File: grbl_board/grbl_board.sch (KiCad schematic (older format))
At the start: 0 parts

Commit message: finished GRBL controller
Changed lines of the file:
@@
 $Descr A4 11693 8268
 encoding utf-8
-Sheet 1 3
+Sheet 1 4
 Title ""
 Date ""
@@
 $EndDescr
 $Sheet
-S 2550 2700 1700 1700
+S 3500 3800 1700 1700
 U 61764DEB
 F0 "grbl_controller" 50
 F1 "grbl_controller.sch" 50
+F2 "RESET" I L 3500 5300 50
+F3 "DIR_X" I R 5200 4000 50
+F4 "DIR_Y" I R 5200 4100 50
+F5 "DIR_Z" I R 5200 4200 50
+F6 "STEP_X" I R 5200 4450 50
+F7 "STEP_Y" I R 5200 4550 50
+F8 "STEP_Z" I R 5200 4650 50
+F9 "LIM_X" I R 5200 4900 50
+F10 "LIM_Y" I R 5200 5000 50
+F11 "LIM_Z" I R 5200 5100 50
+F12 "SPINDLE_DIR" I L 3500 4450 50
+F13 "STEPPER_EN" I R 5200 5300 50
+F14 "COOL_MIST" I L 3500 4100 50
+F15 "RSTABRT" I L 3500 4900 50
+F16 "HOLD" I L 3500 5000 50
+F17 "START" I L 3500 5100 50
+F18 "DOOR_SAFETY" I L 3500 4800 50
+F19 "PROBE" I L 3500 3900 50
+F20 "COOL_FLOOD" I L 3500 4200 50
+F21 "SPINDLE_EN" I L 3500 4550 50
+F22 "SPINDLE_PWM" I L 3500 4350 50
 $EndSheet
 $Sheet
-S 7050 2650 1800 1700
+S 7300 2550 1700 1700
 U 61764E0B
 F0 "stepper_drivers" 50
 F1 "stepper_drivers.sch" 50
 $EndSheet
+$Sheet
+S 3500 1350 1700 1700
+U 619755E7
+F0 "power_supply" 50
+F1 "power_supply.sch" 50
+$EndSheet
 $EndSCHEMATC

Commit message: power supply stage
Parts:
- added J?: 12VDC, symbol Connector:Screw_Terminal_01x02
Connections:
- new net 12VDC: J?.2 (Pin_2)
- new net GND: J?.1 (Pin_1)
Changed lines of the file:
@@
 F0 "power_supply" 50
 F1 "power_supply.sch" 50
+F2 "32VDC" I R 5200 1650 50
+F3 "12VDC" I R 5200 1850 50
+F4 "5VDC" I R 5200 2050 50
 $EndSheet
+$Comp
+L Connector:Screw_Terminal_01x02 J?
+U 1 1 6181440B
+P 1750 1700
+F 0 "J?" H 1668 1375 50  0000 C CNN
+F 1 "12VDC" H 1668 1466 50  0000 C CNN
+F 2 "" H 1750 1700 50  0001 C CNN
+F 3 "~" H 1750 1700 50  0001 C CNN
+	1    1750 1700
+	-1   0    0    1
+$EndComp
+Text Label 5200 1850 0    50   ~ 0
+12VDC
+Text Label 1950 1600 0    50   ~ 0
+12VDC
+$Comp
+L power:GND #PWR?
+U 1 1 61816450
+P 2050 1750
+F 0 "#PWR?" H 2050 1500 50  0001 C CNN
+F 1 "GND" H 2055 1577 50  0000 C CNN
+F 2 "" H 2050 1750 50  0001 C CNN
+F 3 "" H 2050 1750 50  0001 C CNN
+	1    2050 1750
+	1    0    0    -1
+$EndComp
+Wire Wire Line
+	2050 1750 2050 1700
+Wire Wire Line
+	2050 1700 1950 1700
 $EndSCHEMATC

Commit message: motor driver and mcu and limit switches
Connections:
- net 12VDC renamed +12V
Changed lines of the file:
@@
 $Descr A4 11693 8268
 encoding utf-8
-Sheet 1 4
+Sheet 1 6
 Title ""
 Date ""
@@
 $EndSheet
 $Sheet
-S 7300 2550 1700 1700
+S 7050 2450 1700 1700
 U 61764E0B
-F0 "stepper_drivers" 50
-F1 "stepper_drivers.sch" 50
+F0 "aux_mcu" 50
+F1 "aux_mcu.sch" 50
+F2 "X_STEP" I L 7050 2550 50
+F3 "Y_STEP" I L 7050 2650 50
+F4 "Z_STEP" I L 7050 2750 50
+F5 "X_DIR" I L 7050 2900 50
+F6 "Y_DIR" I L 7050 3000 50
+F7 "Z_DIR" I L 7050 3100 50
+F8 "LIM0_IN" I R 8750 3500 50
+F9 "LIM1_IN" I R 8750 3600 50
+F10 "LIM_OUT" I R 8750 3700 50
+F11 "E_DIR_OUT" I R 8750 3300 50
+F12 "X_STEP_OUT" I R 8750 2550 50
+F13 "E_STEP_OUT" I R 8750 2850 50
+F14 "Z_STEP_OUT" I R 8750 2750 50
+F15 "Y_STEP_OUT" I R 8750 2650 50
+F16 "X_DIR_OUT" I R 8750 3000 50
+F17 "Y_DIR_OUT" I R 8750 3100 50
+F18 "Z_DIR_OUT" I R 8750 3200 50
+F19 "MOSI" I L 7050 3800 50
+F20 "MISO" I L 7050 3900 50
+F21 "SCK" I L 7050 4000 50
+F22 "CS0" I L 7050 3300 50
+F23 "CS1" I L 7050 3400 50
+F24 "CS2" I L 7050 3500 50
+F25 "CS3" I L 7050 3600 50
 $EndSheet
 $Sheet
@@
 	-1   0    0    1
 $EndComp
-Text Label 5200 1850 0    50   ~ 0
-12VDC
-Text Label 1950 1600 0    50   ~ 0
-12VDC
 $Comp
 L power:GND #PWR?
@@
 Wire Wire Line
 	2050 1700 1950 1700
+$Sheet
+S 6800 4550 1700 1700
+U 618C57A3
+F0 "stepper_drivers" 50
+F1 "stepper_drivers.sch" 50
+F2 "CS_X" I R 8500 5200 50
+F3 "MISO" I R 8500 4750 50
+F4 "SCK" I R 8500 4950 50
+F5 "MOSI" I R 8500 4850 50
+F6 "VMOT" I L 6800 4850 50
+F7 "EN" I L 6800 4950 50
+F8 "X_STEP" I L 6800 5150 50
+F9 "X_DIR" I L 6800 5650 50
+F10 "CS_Y" I R 8500 5300 50
+F11 "Y_STEP" I L 6800 5250 50
+F12 "Y_DIR" I L 6800 5750 50
+F13 "CS_Z" I R 8500 5400 50
+F14 "Z_STEP" I L 6800 5350 50
+F15 "Z_DIR" I L 6800 5850 50
+F16 "CS_E" I R 8500 5500 50
+F17 "E_STEP" I L 6800 5450 50
+F18 "E_DIR" I L 6800 5950 50
+$EndSheet
+$Comp
+L power:+5V #PWR?
+U 1 1 618E0B3E
+P 5700 2000
+F 0 "#PWR?" H 5700 1850 50  0001 C CNN
+F 1 "+5V" H 5715 2173 50  0000 C CNN
+F 2 "" H 5700 2000 50  0001 C CNN
+F 3 "" H 5700 2000 50  0001 C CNN
+	1    5700 2000
+	1    0    0    -1
+$EndComp
+Wire Wire Line
+	5700 2000 5700 2050
+Wire Wire Line
+	5700 2050 5200 2050
+$Comp
+L power:+12V #PWR?
+U 1 1 618E143D
+P 5550 1800
+F 0 "#PWR?" H 5550 1650 50  0001 C CNN
+F 1 "+12V" H 5565 1973 50  0000 C CNN
+F 2 "" H 5550 1800 50  0001 C CNN
+F 3 "" H 5550 1800 50  0001 C CNN
+	1    5550 1800
+	1    0    0    -1
+$EndComp
+Wire Wire Line
+	5550 1800 5550 1850
+Wire Wire Line
+	5550 1850 5200 1850
+$Comp
+L power:+12V #PWR?
+U 1 1 618E1B94
+P 2250 1550
+F 0 "#PWR?" H 2250 1400 50  0001 C CNN
+F 1 "+12V" H 2265 1723 50  0000 C CNN
+F 2 "" H 2250 1550 50  0001 C CNN
+F 3 "" H 2250 1550 50  0001 C CNN
+	1    2250 1550
+	1    0    0    -1
+$EndComp
+Wire Wire Line
+	2250 1550 2250 1600
+Wire Wire Line
+	2250 1600 1950 1600
+$Sheet
+S 9250 2400 1700 1700
+U 61D39570
+F0 "switch_inputs" 50
+F1 "switch_inputs.sch" 50
+F2 "CYCLE_START" I L 9250 2600 50
+F3 "FEED_HOLD" I L 9250 2700 50
+F4 "RESET_ABORT" I L 9250 2800 50
+F5 "LIM_X" I L 9250 3100 50
+F6 "LIM_Y" I L 9250 3200 50
+F7 "LIM_Z" I L 9250 3300 50
+F8 "LIM_E" I L 9250 3400 50
+F9 "DOOR" I L 9250 3600 50
+$EndSheet
 $EndSCHEMATC

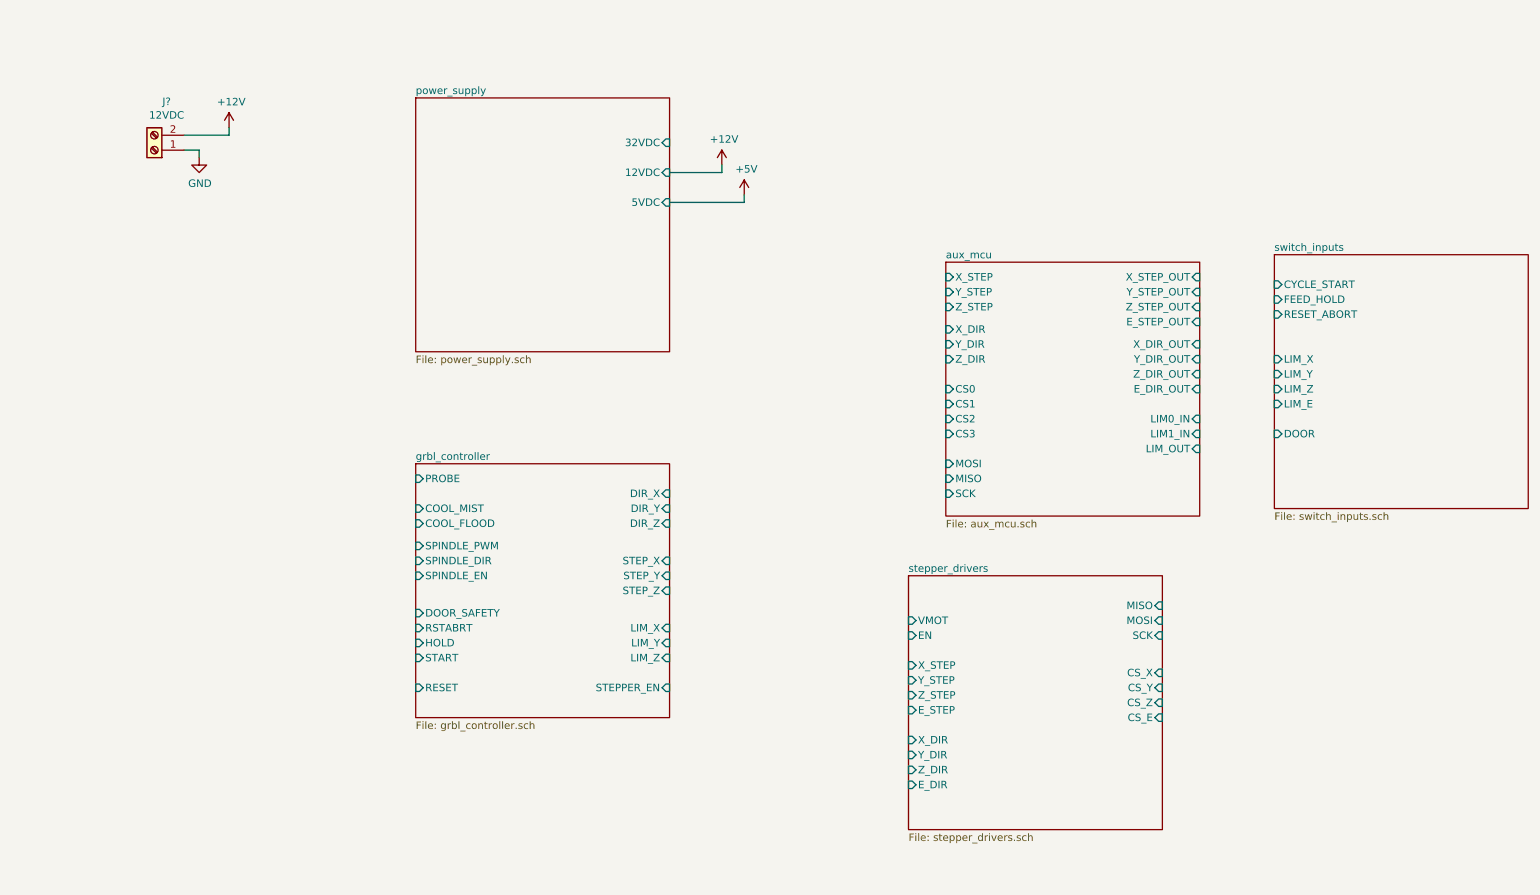
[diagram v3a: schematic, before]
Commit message: changed limit switch control
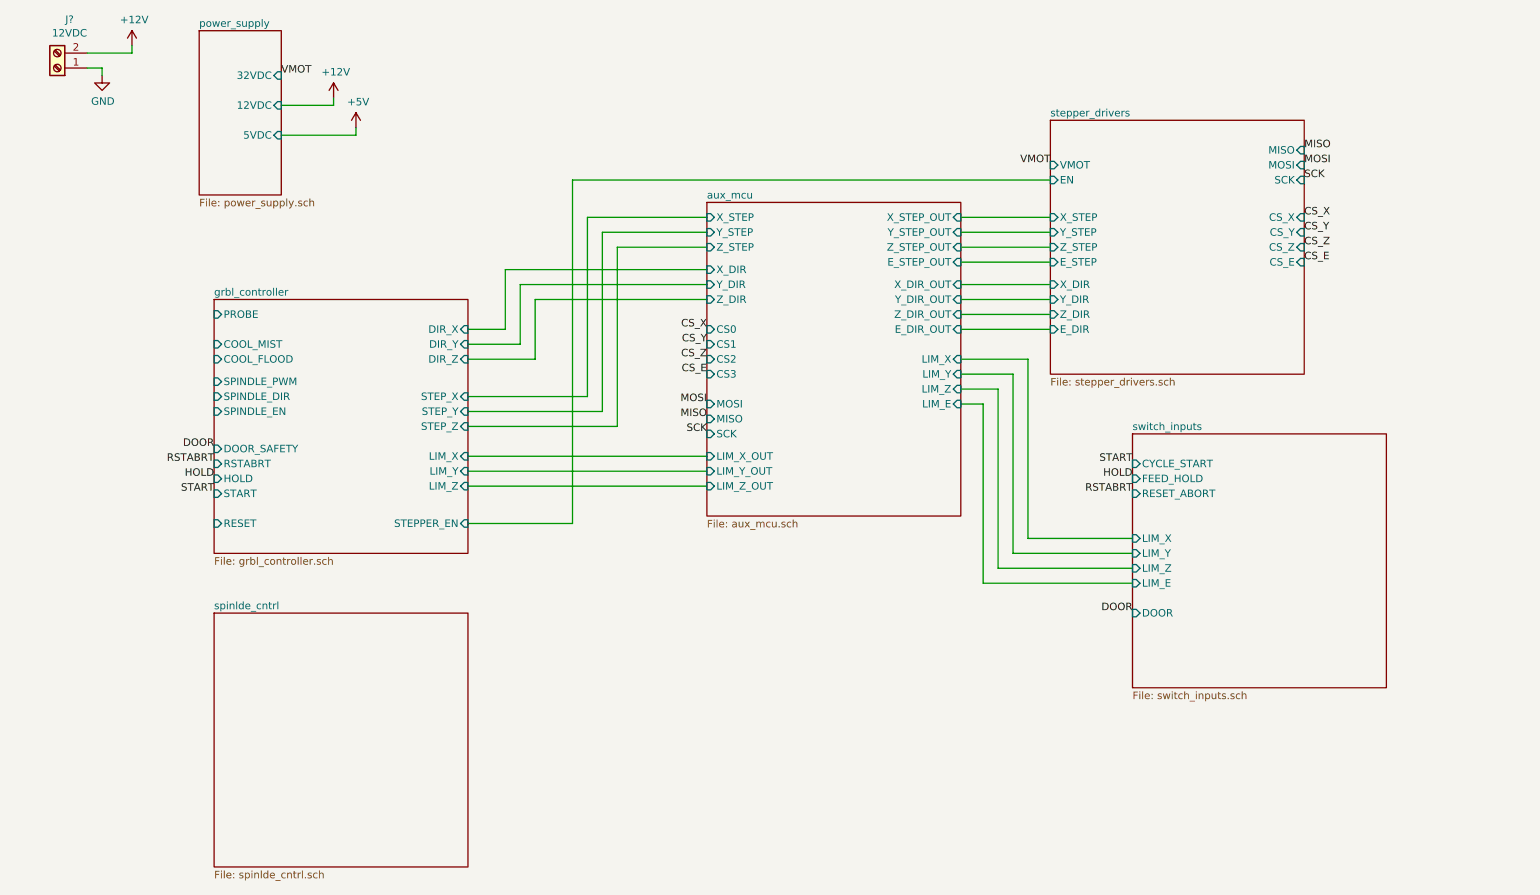
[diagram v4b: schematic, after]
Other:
- moved on the sheet: J?

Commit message: spindle control stage
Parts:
- added J?: COOL, symbol Connector:Screw_Terminal_01x03
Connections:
- net GND: now also J?.1 (Pin_1)
- net grbl_controller/COOL_FLOOD: now also J?.2 (Pin_2)
- net grbl_controller/COOL_MIST: now also J?.3 (Pin_3)
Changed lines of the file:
@@
 F8 "LIM_E" I L 8300 4600 50
 F9 "DOOR" I L 8300 4800 50
+F10 "PROBE" I L 8300 4900 50
 $EndSheet
 $Sheet
@@
 F0 "spinlde_cntrl" 50
 F1 "spinlde_cntrl.sch" 50
+F2 "SPINLDE_PWM" I L 2150 5050 50
+F3 "SPINDLE_EN" I L 2150 5150 50
+F4 "SPINDLE_DIR" I L 2150 5250 50
 $EndSheet
 Text Label 2600 1200 0    50   ~ 0
@@
 Text Label 2150 3800 2    50   ~ 0
 RSTABRT
+Wire Wire Line
+	2150 3250 1650 3250
+Wire Wire Line
+	1650 3250 1650 5050
+Wire Wire Line
+	1650 5050 2150 5050
+Wire Wire Line
+	2150 5150 1550 5150
+Wire Wire Line
+	1550 5150 1550 3450
+Wire Wire Line
+	1550 3450 2150 3450
+Wire Wire Line
+	2150 3350 1450 3350
+Wire Wire Line
+	1450 3350 1450 5250
+Wire Wire Line
+	1450 5250 2150 5250
+Text Label 8300 4900 2    50   ~ 0
+PROBE
+Text Label 2150 2800 2    50   ~ 0
+PROBE
+$Comp
+L Connector:Screw_Terminal_01x03 J?
+U 1 1 6269DFB4
+P 850 3100
+F 0 "J?" H 768 2775 50  0000 C CNN
+F 1 "COOL" H 768 2866 50  0000 C CNN
+F 2 "" H 850 3100 50  0001 C CNN
+F 3 "~" H 850 3100 50  0001 C CNN
+	1    850  3100
+	-1   0    0    1
+$EndComp
+$Comp
+L power:GND #PWR?
+U 1 1 6269EF82
+P 1200 3300
+F 0 "#PWR?" H 1200 3050 50  0001 C CNN
+F 1 "GND" H 1205 3127 50  0000 C CNN
+F 2 "" H 1200 3300 50  0001 C CNN
+F 3 "" H 1200 3300 50  0001 C CNN
+	1    1200 3300
+	1    0    0    -1
+$EndComp
+Wire Wire Line
+	1200 3300 1200 3200
+Wire Wire Line
+	1200 3200 1050 3200
+Wire Wire Line
+	1050 3100 2150 3100
+Wire Wire Line
+	1050 3000 2150 3000
 $EndSCHEMATC

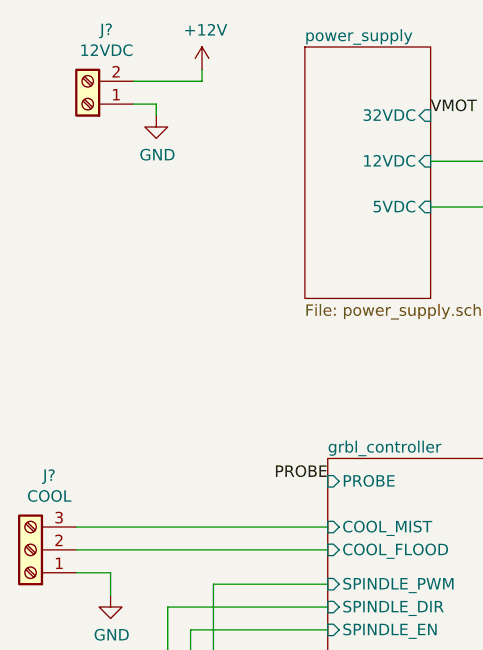
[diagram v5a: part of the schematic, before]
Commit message: added some footprint associations
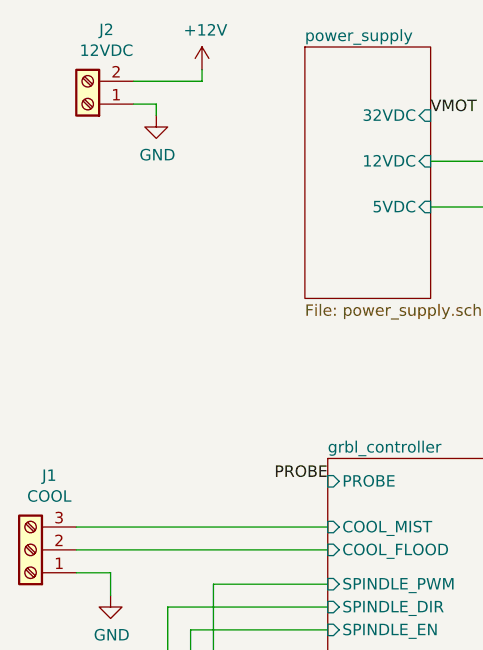
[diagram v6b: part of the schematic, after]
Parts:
- J1: renamed from J?; footprint (none) -> Connector_Phoenix_MC:PhoenixContact_MC_1,5_3-G-3.81_1x03_P3.81mm_Horizontal; Digikey Part No. (none) -> ED2809-ND
- J2: renamed from J?; footprint (none) -> Connector_Phoenix_MC:PhoenixContact_MC_1,5_2-G-3.81_1x02_P3.81mm_Horizontal; Digikey Part No. (none) -> ED2808-ND
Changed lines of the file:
@@
 $EndSheet
 $Comp
-L Connector:Screw_Terminal_01x02 J?
+L Connector:Screw_Terminal_01x02 J2
 U 1 1 6181440B
 P 1100 1150
-F 0 "J?" H 1018 825 50  0000 C CNN
+F 0 "J2" H 1018 825 50  0000 C CNN
 F 1 "12VDC" H 1018 916 50  0000 C CNN
-F 2 "" H 1100 1150 50  0001 C CNN
-F 3 "~" H 1100 1150 50  0001 C CNN
+F 2 "Connector_Phoenix_MC:PhoenixContact_MC_1,5_2-G-3.81_1x02_P3.81mm_Horizontal" H 1100 1150 50  0001 C CNN
+F 3 "https://www.on-shore.com/wp-content/uploads/OSTOQXX3251.pdf" H 1100 1150 50  0001 C CNN
+F 4 "ED2808-ND" H 1100 1150 50  0001 C CNN "Digikey Part No."
 	1    1100 1150
 	-1   0    0    1
 $EndComp
 $Comp
-L power:GND #PWR?
+L power:GND #PWR02
 U 1 1 61816450
 P 1400 1200
-F 0 "#PWR?" H 1400 950 50  0001 C CNN
+F 0 "#PWR02" H 1400 950 50  0001 C CNN
 F 1 "GND" H 1405 1027 50  0000 C CNN
 F 2 "" H 1400 1200 50  0001 C CNN
@@
 $EndSheet
 $Comp
-L power:+5V #PWR?
+L power:+5V #PWR05
 U 1 1 618E0B3E
 P 3100 1550
-F 0 "#PWR?" H 3100 1400 50  0001 C CNN
+F 0 "#PWR05" H 3100 1400 50  0001 C CNN
 F 1 "+5V" H 3115 1723 50  0000 C CNN
 F 2 "" H 3100 1550 50  0001 C CNN
@@
 	3100 1600 2600 1600
 $Comp
-L power:+12V #PWR?
+L power:+12V #PWR04
 U 1 1 618E143D
 P 2950 1350
-F 0 "#PWR?" H 2950 1200 50  0001 C CNN
+F 0 "#PWR04" H 2950 1200 50  0001 C CNN
 F 1 "+12V" H 2965 1523 50  0000 C CNN
 F 2 "" H 2950 1350 50  0001 C CNN
@@
 	2950 1400 2600 1400
 $Comp
-L power:+12V #PWR?
+L power:+12V #PWR03
 U 1 1 618E1B94
 P 1600 1000
-F 0 "#PWR?" H 1600 850 50  0001 C CNN
+F 0 "#PWR03" H 1600 850 50  0001 C CNN
 F 1 "+12V" H 1615 1173 50  0000 C CNN
 F 2 "" H 1600 1000 50  0001 C CNN
@@
 PROBE
 $Comp
-L Connector:Screw_Terminal_01x03 J?
+L Connector:Screw_Terminal_01x03 J1
 U 1 1 6269DFB4
 P 850 3100
-F 0 "J?" H 768 2775 50  0000 C CNN
+F 0 "J1" H 768 2775 50  0000 C CNN
 F 1 "COOL" H 768 2866 50  0000 C CNN
-F 2 "" H 850 3100 50  0001 C CNN
-F 3 "~" H 850 3100 50  0001 C CNN
+F 2 "Connector_Phoenix_MC:PhoenixContact_MC_1,5_3-G-3.81_1x03_P3.81mm_Horizontal" H 850 3100 50  0001 C CNN
+F 3 "https://www.on-shore.com/wp-content/uploads/OSTOQXX3251.pdf" H 850 3100 50  0001 C CNN
+F 4 "ED2809-ND" H 850 3100 50  0001 C CNN "Digikey Part No."
 	1    850  3100
 	-1   0    0    1
 $EndComp
 $Comp
-L power:GND #PWR?
+L power:GND #PWR01
 U 1 1 6269EF82
 P 1200 3300
-F 0 "#PWR?" H 1200 3050 50  0001 C CNN
+F 0 "#PWR01" H 1200 3050 50  0001 C CNN
 F 1 "GND" H 1205 3127 50  0000 C CNN
 F 2 "" H 1200 3300 50  0001 C CNN

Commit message: routing done
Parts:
- added H1, H2, H3, H4: MountingHole, MountingHole:MountingHole_3.2mm_M3_Pad, symbol Mechanical:MountingHole
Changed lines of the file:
@@
 Wire Wire Line
 	1050 3000 2150 3000
+$Comp
+L Mechanical:MountingHole H4
+U 1 1 61BC9E65
+P 4300 1500
+F 0 "H4" H 4400 1546 50  0000 L CNN
+F 1 "MountingHole" H 4400 1455 50  0000 L CNN
+F 2 "MountingHole:MountingHole_3.2mm_M3_Pad" H 4300 1500 50  0001 C CNN
+F 3 "~" H 4300 1500 50  0001 C CNN
+	1    4300 1500
+	1    0    0    -1
+$EndComp
+$Comp
+L Mechanical:MountingHole H3
+U 1 1 61BC8700
+P 4300 1300
+F 0 "H3" H 4400 1346 50  0000 L CNN
+F 1 "MountingHole" H 4400 1255 50  0000 L CNN
+F 2 "MountingHole:MountingHole_3.2mm_M3_Pad" H 4300 1300 50  0001 C CNN
+F 3 "~" H 4300 1300 50  0001 C CNN
+	1    4300 1300
+	1    0    0    -1
+$EndComp
+$Comp
+L Mechanical:MountingHole H2
+U 1 1 61BC6C16
+P 4300 1100
+F 0 "H2" H 4400 1146 50  0000 L CNN
+F 1 "MountingHole" H 4400 1055 50  0000 L CNN
+F 2 "MountingHole:MountingHole_3.2mm_M3_Pad" H 4300 1100 50  0001 C CNN
+F 3 "~" H 4300 1100 50  0001 C CNN
+	1    4300 1100
+	1    0    0    -1
+$EndComp
+$Comp
+L Mechanical:MountingHole H1
+U 1 1 61BC6044
+P 4300 900
+F 0 "H1" H 4400 946 50  0000 L CNN
+F 1 "MountingHole" H 4400 855 50  0000 L CNN
+F 2 "MountingHole:MountingHole_3.2mm_M3_Pad" H 4300 900 50  0001 C CNN
+F 3 "~" H 4300 900 50  0001 C CNN
+	1    4300 900
+	1    0    0    -1
+$EndComp
 $EndSCHEMATC

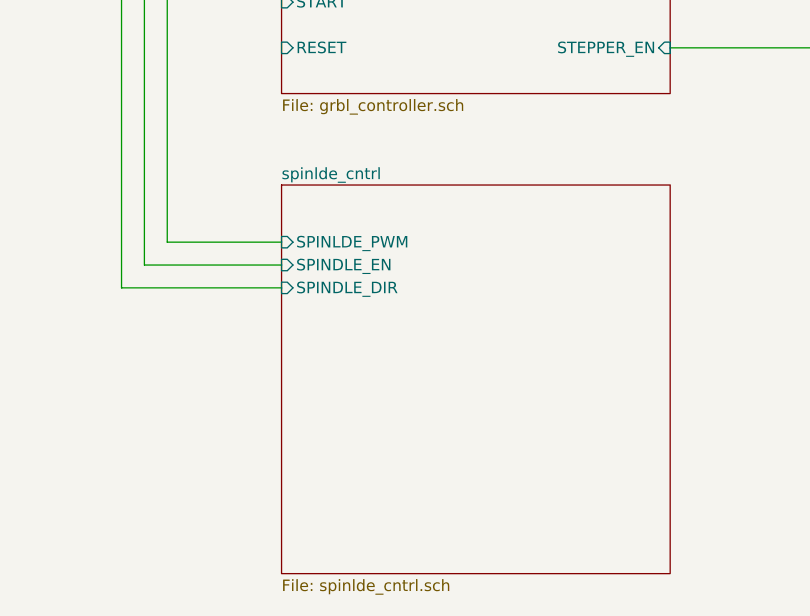
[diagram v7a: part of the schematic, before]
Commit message: fixed limit switch disconnect issue
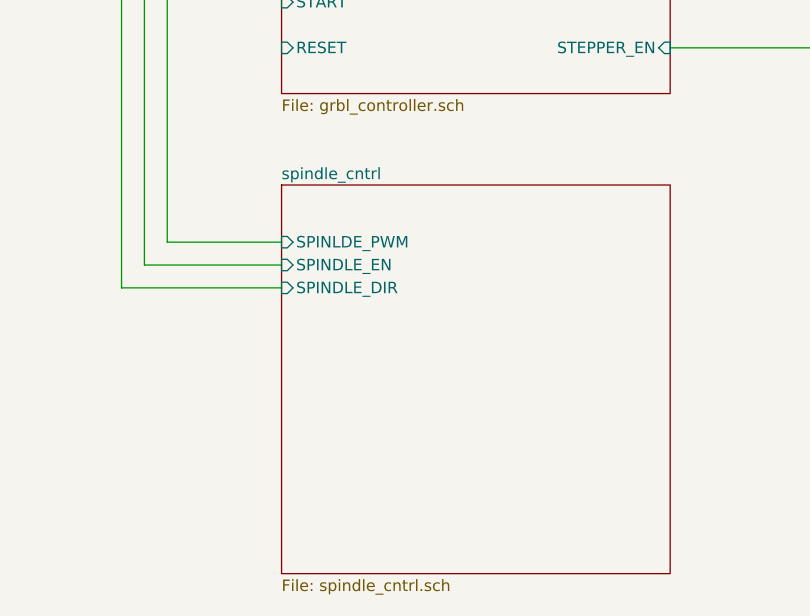
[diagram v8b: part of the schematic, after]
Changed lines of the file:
@@
 S 2150 4800 1700 1700
 U 61DA711F
-F0 "spinlde_cntrl" 50
-F1 "spinlde_cntrl.sch" 50
+F0 "spindle_cntrl" 50
+F1 "spindle_cntrl.sch" 50
 F2 "SPINLDE_PWM" I L 2150 5050 50
 F3 "SPINDLE_EN" I L 2150 5150 50
